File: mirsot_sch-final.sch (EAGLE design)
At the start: 43 parts, among them IC1 7805DT, U2 ATMEGA16-16AC, U4 DRV8833PWPR

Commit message: shifted from smd to tht
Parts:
- removed 3.3V_LED, 5V_LED, VCC_LED: RED, adafruit:LEDCHIPLED_0603
- removed C10: 10u, rcl:C-USC0603
- removed C2: 100n, rcl:C-USC0603
- removed CN1: (no value), adafruit:JST_2PIN-THM
- removed LED_1, LED_2, LED_3, LED_4, LED_5: GREEN, adafruit:LEDCHIPLED_0603
- removed R3: 43k, rcl:R-US_R1206
- removed S1: (no value), switch-omron:10-XX
- removed U2: ATMEGA16-16AC, ATMEGA16-16AC:ATMEGA16-16AC
- added 3V3LD, 5VLD, BATT: RED, led:LEDSML1206
- added C12, C14: 22pF, rcl:C-US025-025X050
- added C15: 100n, rcl:C-US025-024X044
- added IC2: MEGA16-P, atmel:MEGA16-P
- added LD1, LD2, LD3: GREEN, led:LEDSML1206
- added M1: WIRELESS-NRF24L01, diy-modules:WIRELESS-NRF24L01
- added Q2: (no value), crystal:CRYSTALHC49S
- added R13: 43k, rcl:R-US_M1206
- added RX: BLUE, led:LEDSML1206
- added S2: (no value), switch-omron:10-XX
- added TX: YELLOW, led:LEDSML1206
- C1, C13, C3, C6: device rcl:C-USC0603 -> rcl:C-USC1206K
- C4, C5, C9: device rcl:C-USC0603 -> rcl:C-USC0603K
- C8: value 100n -> 10u; device rcl:C-USC0603 -> rcl:C-USC1206K
- IC1: value 7805DT -> 7805T; device linear:7805DT -> linear:7805T
- JP1: device pinhead:PINHD-2X3 -> pinhead:PINHD-2X3/90
- JP2: device pinhead:PINHD-1X3 -> pinhead:PINHD-1X3/90
- JP3: device adafruit:PINHD-2X4 -> pinhead:PINHD-1X3/90
- R1, R10, R11, R12, R2, R4, R6, R7, R8, R9: device rcl:R-US_R1206 -> rcl:R-US_M1206
- R5: device rcl:R-US_R2512 -> rcl:R-US_M1206
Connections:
- removed net N$1: CN1.1, CN2.2
- removed net RX_LED: LED_4.C, U2.(RXD)_PD0
- removed net TX_LED: LED_5.C, U2.(TXD)_PD1
- new net GND1: C15.2
- new net N$12: C12.1, IC2.XTAL2, Q2.2
- new net N$13: C14.1, IC2.XTAL1, Q2.1
- new net N$14: C12.2, C14.2
- new net RESET: JP1.5, JP3.2
- new net RX: IC2.(RXD)PD0, JP3.1, RX.C
- new net TX: IC2.(TXD)PD1, JP3.3, TX.C
- net +3V3: now also C8.1, M1.VCC; no longer C10.1, JP3.2
- net +5V: now also C15.1, IC2.AREF, IC2.AVCC, IC2.VCC, R13.2; no longer C8.1, R3.2, U2.AREF, U2.AVCC, U2.VCC, U2.VCC_2, U2.VCC_3
- net AIN1: now also IC2.(AIN1/OC0)PB3; no longer U2.PB3_(AIN1/OC0)
- net AIN2: now also IC2.(OC1B)PD4; no longer U2.(OC1B)_PD4
- net BIN1: now also IC2.(OC1A)PD5; no longer U2.(OC1A)_PD5
- net BIN2: now also IC2.(OC2)PD7; no longer U2.(OC2)_PD7
- net CE: now also IC2.(TOSC1)PC6, M1.CE; no longer JP3.3, U2.PC6_(TOSC1)
- net CSN: now also IC2.(TOSC2)PC7, M1.CSN; no longer JP3.4, U2.PC7_(TOSC2)
- net ENB: now also IC2.(INT1)PD3; no longer U2.(INT1)_PD3
- net ENCD_MA_1: now also IC2.(TCK)PC2; no longer U2.(TCK)_PC2
- net ENCD_MA_2: now also IC2.(TMS)PC3; no longer U2.(TMS)_PC3
- net ENCD_MB_1: now also IC2.(TDO)PC4; no longer U2.PC4_(TDO)
- net ENCD_MB_2: now also IC2.(TDI)PC5; no longer U2.PC5_(TDI)
- net GND: now also 3V3LD.C, 5VLD.C, BATT.C, IC2.GND, IC2.GND@1, LD1.C, LD2.C, LD3.C, M1.GND, S2.S, S2.S1; no longer 3.3V_LED.C, 5V_LED.C, C10.2, C2.2, JP3.1, LED_1.C, LED_2.C, LED_3.C, S1.S, S1.S1, U2.GND, U2.GND_2, U2.GND_3, U2.GND_4, VCC_LED.C
- net IRQ: now also IC2.(AIN0/INT2)PB2, M1.IRQ; no longer JP3.8, U2.PB2_(AIN0/INT2)
- net LED_1: now also IC2.(T0/XCK)PB0; no longer U2.PB0_(XCK/T0)
- net LED_2: now also IC2.(T1)PB1; no longer U2.PB1_(T1)
- net LED_3: now also IC2.(SS)PB4; no longer U2.PB4_(~SS)
- net MISO: now also IC2.(MISO)PB6, M1.MISO; no longer JP3.7, U2.(MISO)_PB6
- net MOSI: now also IC2.(MOSI)PB5, M1.MOSI; no longer JP3.6, U2.(MOSI)_PB5
- net N$10: now also RX.A; no longer LED_4.A
- net N$11: now also TX.A; no longer LED_5.A
- net N$2: now also BATT.A; no longer VCC_LED.A
- net N$3: now also LD1.A; no longer LED_1.A
- net N$4: now also LD2.A; no longer LED_2.A
- net N$5: now also 5VLD.A; no longer 5V_LED.A
- net N$6: now also 3V3LD.A; no longer 3.3V_LED.A
- net N$9: now also LD3.A; no longer LED_3.A
- net RST: now also IC2.RESET, R13.1, S2.P, S2.P1; no longer JP1.5, R3.1, S1.P, S1.P1, U2.~RESET
- net SCK: now also IC2.(SCK)PB7, M1.SCK; no longer JP3.5, U2.(SCK)_PB7
- net VCC: now also CN2.2; no longer C2.1, CN1.2
- net VCC_REF: now also IC2.(ADC0)PA0; no longer U2.PA0_(ADC0)
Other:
- moved on the sheet: C8, CN2, R1, R7

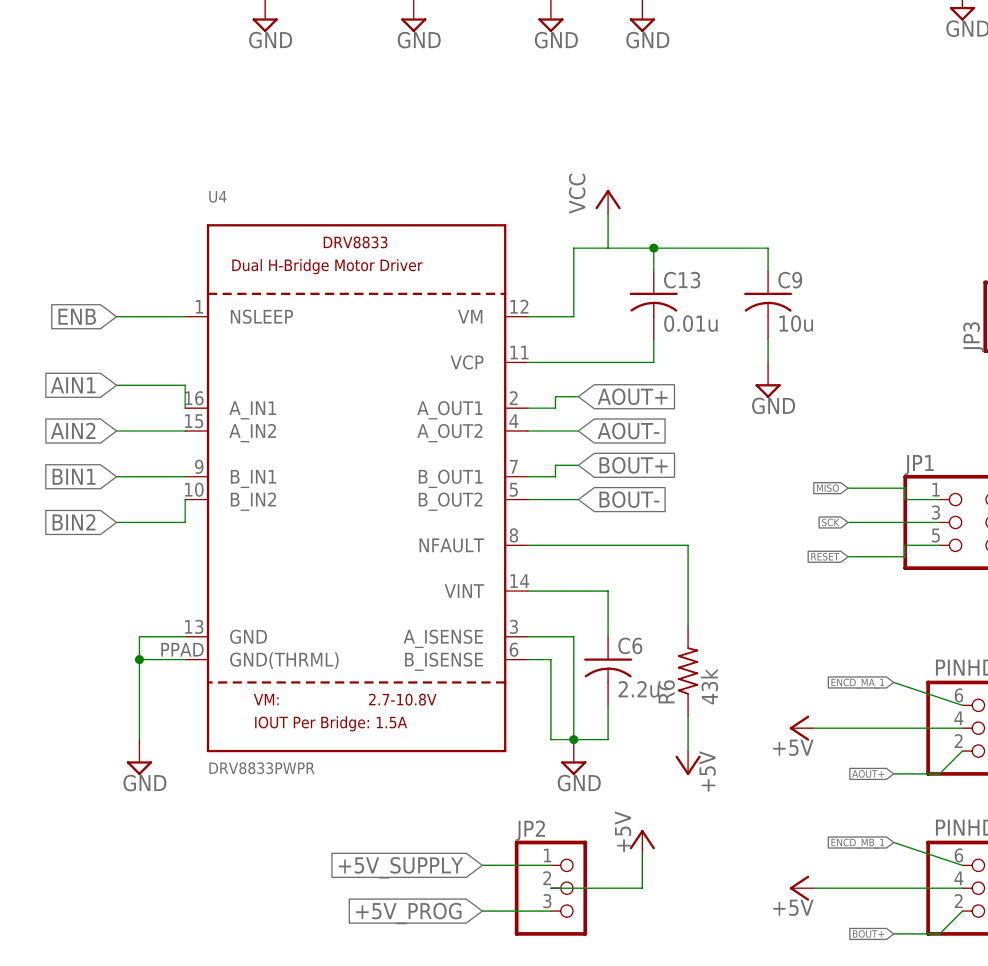
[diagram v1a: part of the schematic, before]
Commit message: added drv8833 module
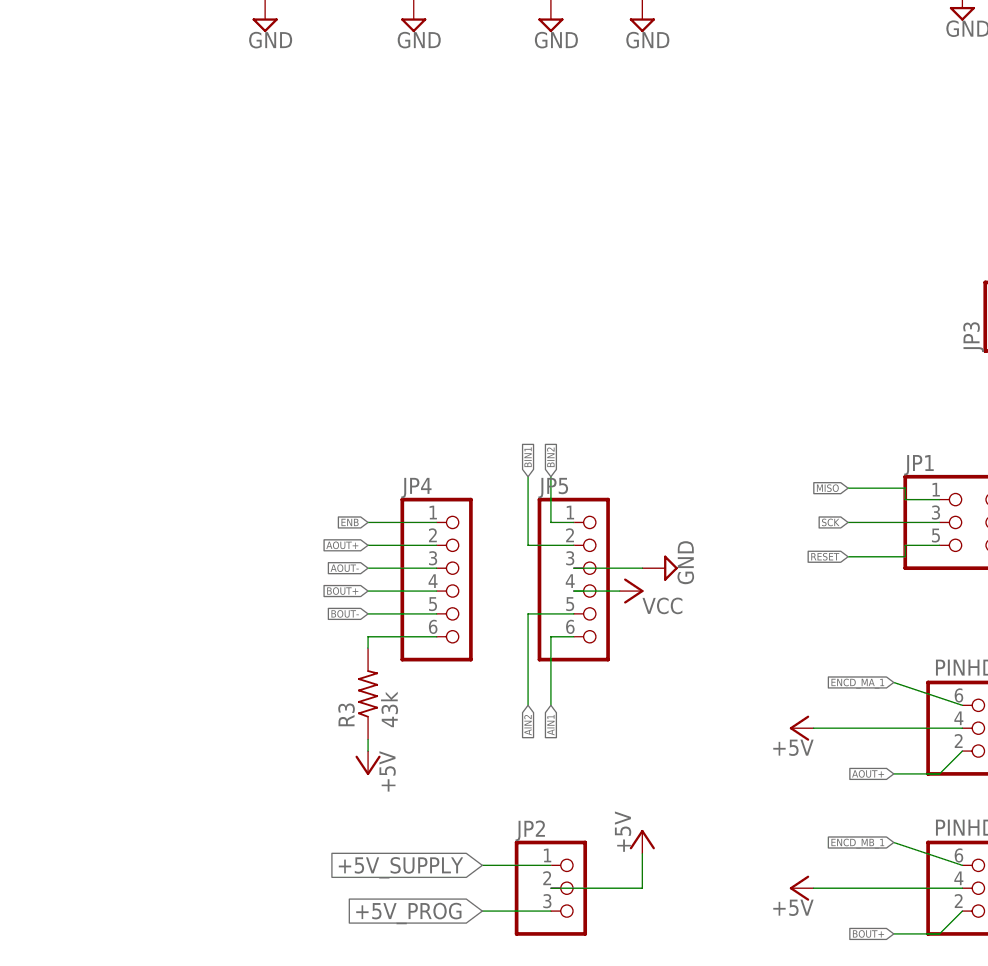
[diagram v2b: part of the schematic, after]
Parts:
- removed C13: 0.01u, rcl:C-USC1206K
- removed C6: 2.2u, rcl:C-USC1206K
- removed C9: 10u, rcl:C-USC0603K
- removed R6: 43k, rcl:R-US_M1206
- removed U4: DRV8833PWPR, microbuilder:DRV8833
- added JP4, JP5: (no value), pinhead:PINHD-1X6
- added R3: 43k, rcl:R-US_M1206
- C15: device rcl:C-US025-024X044 -> rcl:C-USC0603K
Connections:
- removed net N$7: C13.2, U4.VCP
- removed net N$8: C6.1, U4.VINT
- removed net NFAULT: R6.2, U4.NFAULT
- new net N$1: JP4.6, R3.2
- net +5V: now also R3.1; no longer R6.1
- net AIN1: now also JP5.6; no longer U4.A_IN1
- net AIN2: now also JP5.5; no longer U4.A_IN2
- net AOUT+: now also JP4.2; no longer U4.A_OUT1
- net AOUT-: now also JP4.3; no longer U4.A_OUT2
- net BIN1: now also JP5.2; no longer U4.B_IN1
- net BIN2: now also JP5.1; no longer U4.B_IN2
- net BOUT+: now also JP4.4; no longer U4.B_OUT1
- net BOUT-: now also JP4.5; no longer U4.B_OUT2
- net ENB: now also JP4.1; no longer U4.NSLEEP
- net GND: now also JP5.3; no longer C6.2, C9.2, U4.A_ISENSE, U4.B_ISENSE, U4.GND(THRML), U4.GND@1
- net VCC: now also JP5.4; no longer C13.1, C9.1, U4.VM

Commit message: Routing Done
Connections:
- removed net GND1: C15.2
- net ENB: now also IC2.(SCL)PC0; no longer IC2.(INT1)PD3
- net ENCD_MA_1: now also IC2.(TMS)PC3; no longer IC2.(TCK)PC2
- net ENCD_MA_2: now also IC2.(TCK)PC2; no longer IC2.(TMS)PC3
- net ENCD_MB_1: now also IC2.(SDA)PC1; no longer IC2.(TDO)PC4
- net ENCD_MB_2: now also IC2.(TDO)PC4; no longer IC2.(TDI)PC5
- net GND: now also C15.2
- net LED_1: now also IC2.(ICP)PD6; no longer IC2.(T0/XCK)PB0
- net LED_2: now also IC2.(INT1)PD3; no longer IC2.(T1)PB1
- net LED_3: now also IC2.(INT0)PD2; no longer IC2.(SS)PB4
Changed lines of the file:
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@@
 </instance>
 <instance part="JP3" gate="A" x="99.06" y="45.72" smashed="yes" rot="R90">
-<attribute name="NAME" x="93.345" y="39.37" size="1.778" layer="95" rot="R90"/>
 <attribute name="VALUE" x="106.68" y="39.37" size="1.778" layer="96" rot="R90"/>
 </instance>
@@
 <wire x1="55.88" y1="15.24" x2="48.26" y2="15.24" width="0.1524" layer="91"/>
 </segment>
+<segment>
+<pinref part="C15" gate="G$1" pin="2"/>
+<pinref part="SUPPLY24" gate="GND" pin="GND"/>
+<wire x1="156.718" y1="-3.81" x2="156.718" y2="-5.08" width="0.1524" layer="91"/>
+</segment>
 </net>
 <net name="BIN2" class="0">
@@
 <net name="ENB" class="0">
 <segment>
-<wire x1="218.44" y1="-43.18" x2="222.25" y2="-43.18" width="0.1524" layer="91"/>
-<label x="222.25" y="-43.18" size="0.8128" layer="95" rot="MR180" xref="yes"/>
-<pinref part="IC2" gate="G$1" pin="(INT1)PD3"/>
-</segment>
-<segment>
 <pinref part="JP4" gate="A" pin="1"/>
 <wire x1="33.02" y1="20.32" x2="25.4" y2="20.32" width="0.1524" layer="91"/>
 <label x="25.4" y="20.32" size="0.8128" layer="95" rot="R180" xref="yes"/>
+</segment>
+<segment>
+<pinref part="IC2" gate="G$1" pin="(SCL)PC0"/>
+<wire x1="218.44" y1="-27.94" x2="220.98" y2="-27.94" width="0.1524" layer="91"/>
+<label x="220.98" y="-27.94" size="1.778" layer="95" xref="yes"/>
 </segment>
 </net>
@@
 </segment>
 <segment>
-<wire x1="220.98" y1="-22.86" x2="218.44" y2="-22.86" width="0.1524" layer="91"/>
-<label x="220.98" y="-22.86" size="0.8128" layer="95" rot="MR180" xref="yes"/>
-<pinref part="IC2" gate="G$1" pin="(TCK)PC2"/>
+<pinref part="IC2" gate="G$1" pin="(TMS)PC3"/>
+<wire x1="218.44" y1="-20.32" x2="220.98" y2="-20.32" width="0.1524" layer="91"/>
+<label x="220.98" y="-20.32" size="1.778" layer="95" xref="yes"/>
 </segment>
 </net>
@@
 </segment>
 <segment>
-<wire x1="218.44" y1="-17.78" x2="220.98" y2="-17.78" width="0.1524" layer="91"/>
-<label x="220.98" y="-17.78" size="0.8128" layer="95" rot="MR180" xref="yes"/>
-<pinref part="IC2" gate="G$1" pin="(TDO)PC4"/>
+<pinref part="IC2" gate="G$1" pin="(SDA)PC1"/>
+<wire x1="218.44" y1="-25.4" x2="220.98" y2="-25.4" width="0.1524" layer="91"/>
+<label x="220.98" y="-25.4" size="1.778" layer="95" xref="yes"/>
 </segment>
 </net>
@@
 </segment>
 <segment>
-<wire x1="220.98" y1="-20.32" x2="218.44" y2="-20.32" width="0.1524" layer="91"/>
-<label x="220.98" y="-20.32" size="0.8128" layer="95" rot="MR180" xref="yes"/>
-<pinref part="IC2" gate="G$1" pin="(TMS)PC3"/>
+<pinref part="IC2" gate="G$1" pin="(TCK)PC2"/>
+<wire x1="218.44" y1="-22.86" x2="220.98" y2="-22.86" width="0.1524" layer="91"/>
+<label x="220.98" y="-22.86" size="1.778" layer="95" xref="yes"/>
 </segment>
 </net>
@@
 </segment>
 <segment>
-<wire x1="220.98" y1="-15.24" x2="218.44" y2="-15.24" width="0.1524" layer="91"/>
-<label x="220.98" y="-15.24" size="0.8128" layer="95" rot="MR180" xref="yes"/>
-<pinref part="IC2" gate="G$1" pin="(TDI)PC5"/>
+<pinref part="IC2" gate="G$1" pin="(TDO)PC4"/>
+<wire x1="218.44" y1="-17.78" x2="220.98" y2="-17.78" width="0.1524" layer="91"/>
+<label x="220.98" y="-17.78" size="1.778" layer="95" xref="yes"/>
 </segment>
 </net>
@@
 </segment>
 <segment>
-<wire x1="218.44" y1="-5.08" x2="220.98" y2="-5.08" width="0.1524" layer="91"/>
-<label x="220.98" y="-5.08" size="0.8128" layer="95" xref="yes"/>
-<pinref part="IC2" gate="G$1" pin="(T0/XCK)PB0"/>
+<pinref part="IC2" gate="G$1" pin="(ICP)PD6"/>
+<wire x1="218.44" y1="-35.56" x2="220.98" y2="-35.56" width="0.1524" layer="91"/>
+<label x="220.98" y="-35.56" size="1.778" layer="95" xref="yes"/>
 </segment>
 </net>
@@
 </segment>
 <segment>
-<wire x1="218.44" y1="-2.54" x2="220.98" y2="-2.54" width="0.1524" layer="91"/>
-<label x="220.98" y="-2.54" size="0.8128" layer="95" xref="yes"/>
-<pinref part="IC2" gate="G$1" pin="(T1)PB1"/>
+<pinref part="IC2" gate="G$1" pin="(INT1)PD3"/>
+<wire x1="218.44" y1="-43.18" x2="220.98" y2="-43.18" width="0.1524" layer="91"/>
+<label x="220.98" y="-43.18" size="1.778" layer="95" xref="yes"/>
 </segment>
 </net>
@@
 </segment>
 <segment>
-<wire x1="218.44" y1="5.08" x2="220.98" y2="5.08" width="0.1524" layer="91"/>
-<label x="220.98" y="5.08" size="0.8128" layer="95" xref="yes"/>
-<pinref part="IC2" gate="G$1" pin="(SS)PB4"/>
+<pinref part="IC2" gate="G$1" pin="(INT0)PD2"/>
+<wire x1="218.44" y1="-45.72" x2="220.98" y2="-45.72" width="0.1524" layer="91"/>
+<label x="220.98" y="-45.72" size="1.778" layer="95" xref="yes"/>
 </segment>
 </net>
@@
 </segment>
 </net>
-<net name="GND1" class="0">
-<segment>
-<wire x1="156.718" y1="-3.81" x2="156.718" y2="-5.08" width="0.1524" layer="91"/>
-<pinref part="C15" gate="G$1" pin="2"/>
-<pinref part="SUPPLY24" gate="GND" pin="GND"/>
-</segment>
-</net>
 <net name="N$1" class="0">
 <segment>
@@
 </sheet>
 </sheets>
-<errors>
-</errors>
 </schematic>
 </drawing>
